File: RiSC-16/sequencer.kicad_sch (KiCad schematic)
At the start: 4 parts, among them U12 KM28C64A, U13 KM28C64A, U14 74LS273, U15 74LS273

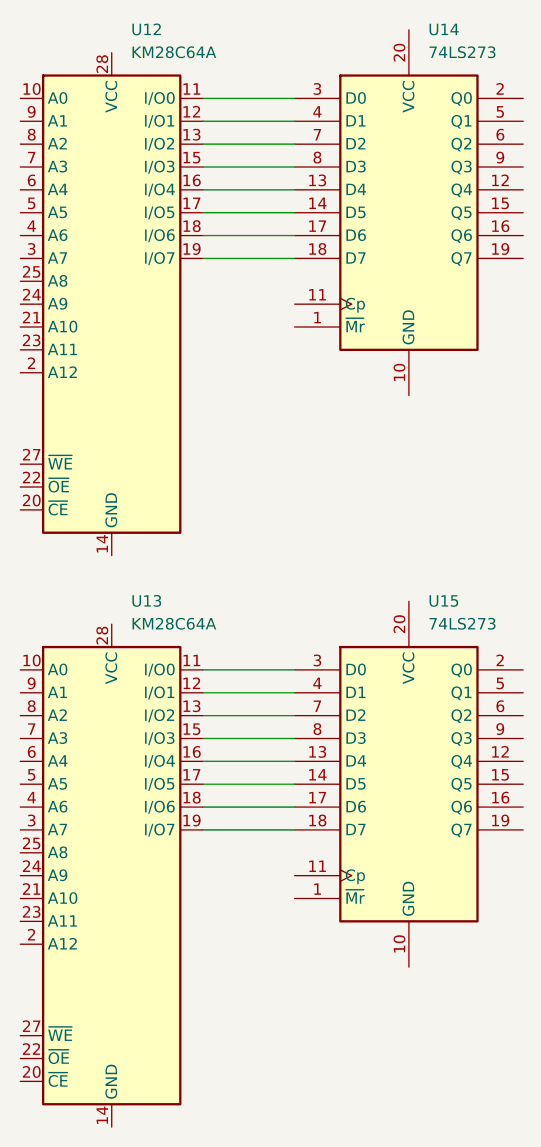
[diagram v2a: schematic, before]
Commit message: Added a custom symbol for the AM29705. Reworked to use it in two different approaches.
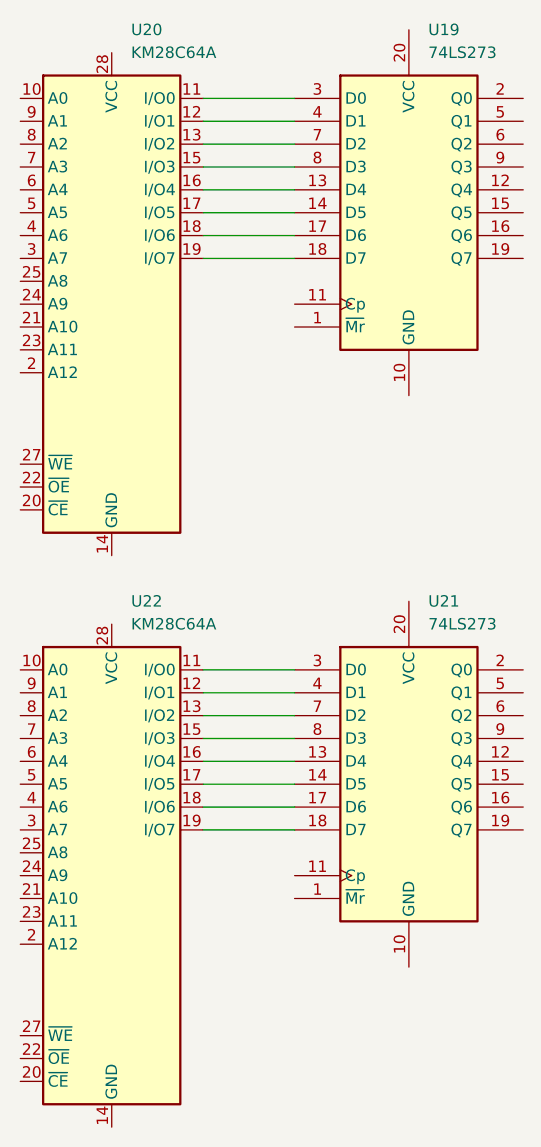
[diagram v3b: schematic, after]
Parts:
- renumbered U14 to U19, U12 to U20, U15 to U21, U13 to U22
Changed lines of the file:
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@@
 		(dnp no)
 		(fields_autoplaced yes)
-		(property "Reference" "U13"
+		(property "Reference" "U22"
 			(at 88.5033 83.82 0)
 			(effects
@@
 			(project ""
 				(path "/09ce4153-429f-4803-b069-3af485a81dd6/484a2b1a-2f0b-4860-b5b9-2f2af10857fa"
-					(reference "U13")
+					(reference "U22")
 					(unit 1)
 				)
@@
 		(dnp no)
 		(fields_autoplaced yes)
-		(property "Reference" "U12"
+		(property "Reference" "U20"
 			(at 88.5033 20.32 0)
 			(effects
@@
 			(project ""
 				(path "/09ce4153-429f-4803-b069-3af485a81dd6/484a2b1a-2f0b-4860-b5b9-2f2af10857fa"
-					(reference "U12")
+					(reference "U20")
 					(unit 1)
 				)
@@
 		(dnp no)
 		(fields_autoplaced yes)
-		(property "Reference" "U15"
+		(property "Reference" "U21"
 			(at 121.5233 83.82 0)
 			(effects
@@
 			(project ""
 				(path "/09ce4153-429f-4803-b069-3af485a81dd6/484a2b1a-2f0b-4860-b5b9-2f2af10857fa"
-					(reference "U15")
+					(reference "U21")
 					(unit 1)
 				)
@@
 		(dnp no)
 		(fields_autoplaced yes)
-		(property "Reference" "U14"
+		(property "Reference" "U19"
 			(at 121.5233 20.32 0)
 			(effects
@@
 			(project ""
 				(path "/09ce4153-429f-4803-b069-3af485a81dd6/484a2b1a-2f0b-4860-b5b9-2f2af10857fa"
-					(reference "U14")
+					(reference "U19")
 					(unit 1)
 				)

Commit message: Check point of design.
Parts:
- renumbered U19 to U22, U20 to U23, U21 to U24, U22 to U25
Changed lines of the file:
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@@
 		(dnp no)
 		(fields_autoplaced yes)
-		(property "Reference" "U22"
+		(property "Reference" "U25"
 			(at 88.5033 83.82 0)
 			(effects
@@
 			(project ""
 				(path "/09ce4153-429f-4803-b069-3af485a81dd6/484a2b1a-2f0b-4860-b5b9-2f2af10857fa"
-					(reference "U22")
+					(reference "U25")
 					(unit 1)
 				)
@@
 		(dnp no)
 		(fields_autoplaced yes)
-		(property "Reference" "U20"
+		(property "Reference" "U23"
 			(at 88.5033 20.32 0)
 			(effects
@@
 			(project ""
 				(path "/09ce4153-429f-4803-b069-3af485a81dd6/484a2b1a-2f0b-4860-b5b9-2f2af10857fa"
-					(reference "U20")
+					(reference "U23")
 					(unit 1)
 				)
@@
 		(dnp no)
 		(fields_autoplaced yes)
-		(property "Reference" "U21"
+		(property "Reference" "U24"
 			(at 121.5233 83.82 0)
 			(effects
@@
 			(project ""
 				(path "/09ce4153-429f-4803-b069-3af485a81dd6/484a2b1a-2f0b-4860-b5b9-2f2af10857fa"
-					(reference "U21")
+					(reference "U24")
 					(unit 1)
 				)
@@
 		(dnp no)
 		(fields_autoplaced yes)
-		(property "Reference" "U19"
+		(property "Reference" "U22"
 			(at 121.5233 20.32 0)
 			(effects
@@
 			(project ""
 				(path "/09ce4153-429f-4803-b069-3af485a81dd6/484a2b1a-2f0b-4860-b5b9-2f2af10857fa"
-					(reference "U19")
+					(reference "U22")
 					(unit 1)
 				)

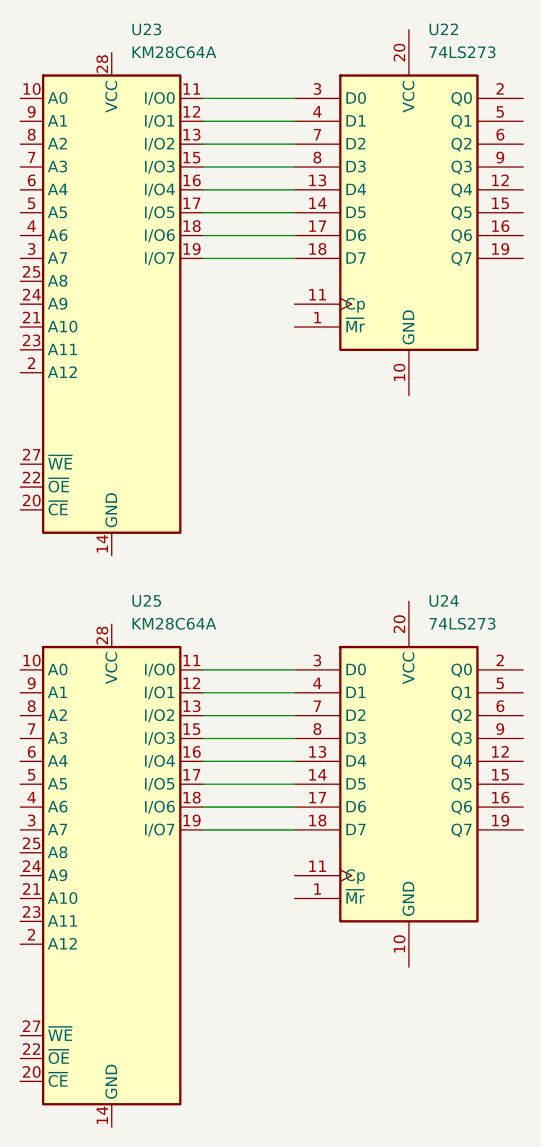
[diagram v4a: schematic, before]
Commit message: Annotated the schematic to align part numbers. EPROM and RAM board was added last revision. Reworked the src1 latching to assert 0xf to select the PC.
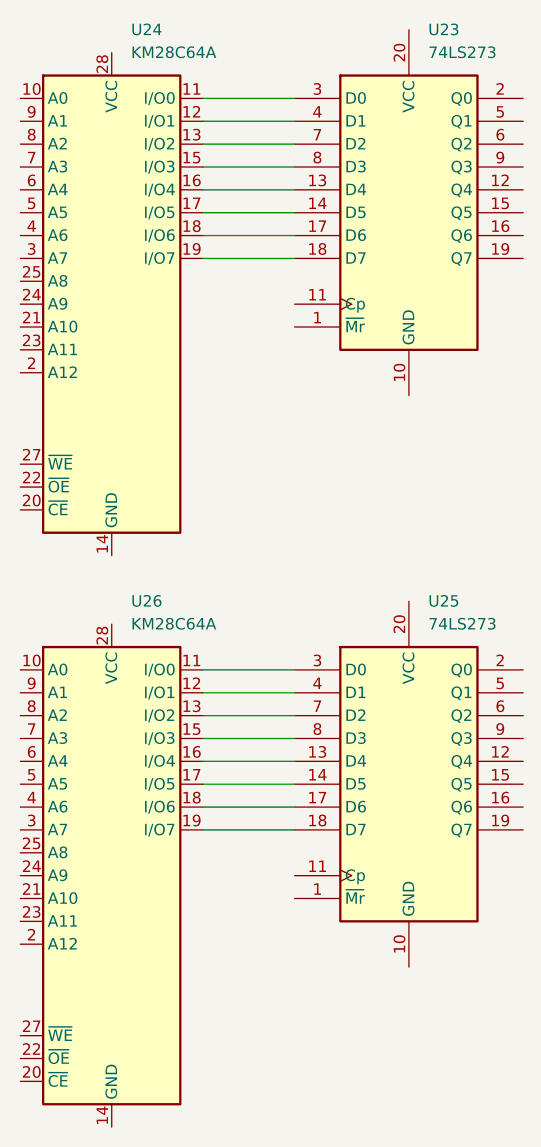
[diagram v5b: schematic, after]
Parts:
- renumbered U22 to U23, U23 to U24, U24 to U25, U25 to U26
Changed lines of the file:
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@@
 		(dnp no)
 		(fields_autoplaced yes)
-		(property "Reference" "U25"
+		(property "Reference" "U26"
 			(at 88.5033 83.82 0)
 			(effects
@@
 			(project ""
 				(path "/09ce4153-429f-4803-b069-3af485a81dd6/484a2b1a-2f0b-4860-b5b9-2f2af10857fa"
-					(reference "U25")
+					(reference "U26")
 					(unit 1)
 				)
@@
 		(dnp no)
 		(fields_autoplaced yes)
-		(property "Reference" "U23"
+		(property "Reference" "U24"
 			(at 88.5033 20.32 0)
 			(effects
@@
 			(project ""
 				(path "/09ce4153-429f-4803-b069-3af485a81dd6/484a2b1a-2f0b-4860-b5b9-2f2af10857fa"
-					(reference "U23")
+					(reference "U24")
 					(unit 1)
 				)
@@
 		(dnp no)
 		(fields_autoplaced yes)
-		(property "Reference" "U24"
+		(property "Reference" "U25"
 			(at 121.5233 83.82 0)
 			(effects
@@
 			(project ""
 				(path "/09ce4153-429f-4803-b069-3af485a81dd6/484a2b1a-2f0b-4860-b5b9-2f2af10857fa"
-					(reference "U24")
+					(reference "U25")
 					(unit 1)
 				)
@@
 		(dnp no)
 		(fields_autoplaced yes)
-		(property "Reference" "U22"
+		(property "Reference" "U23"
 			(at 121.5233 20.32 0)
 			(effects
@@
 			(project ""
 				(path "/09ce4153-429f-4803-b069-3af485a81dd6/484a2b1a-2f0b-4860-b5b9-2f2af10857fa"
-					(reference "U22")
+					(reference "U23")
 					(unit 1)
 				)
